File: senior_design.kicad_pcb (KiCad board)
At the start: 2 copper layers, 128.6 x 80.8 mm, 95 parts, among them J1 Conn_ARM_JTAG_SWD_20, J2 Conn_01x03_Pin, J4 USB_B_Micro, J5 Out_to_display, SW1 SW_SPST, U1 Boost Converter - TPS61169DCKR, U11 NCP1117-3.3_SOT223, U2 OPA196xDGK, U3 RA8875L3N, U4 OPA196xDGK, U5 M24C64-WMN6TP, U6 STM32F469VETx, U7 74HC4050D, Y1 20MHz

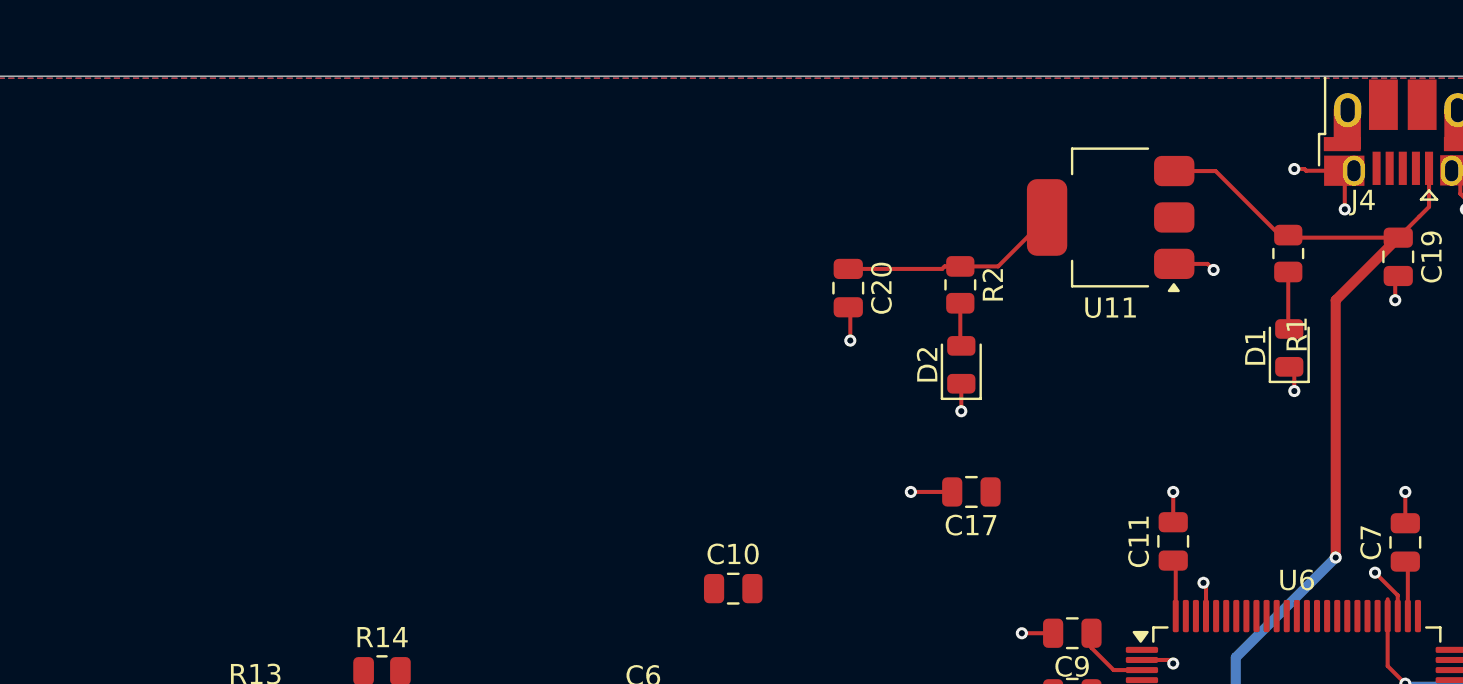
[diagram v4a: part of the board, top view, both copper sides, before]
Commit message: Updated Audio Schematic & PCB
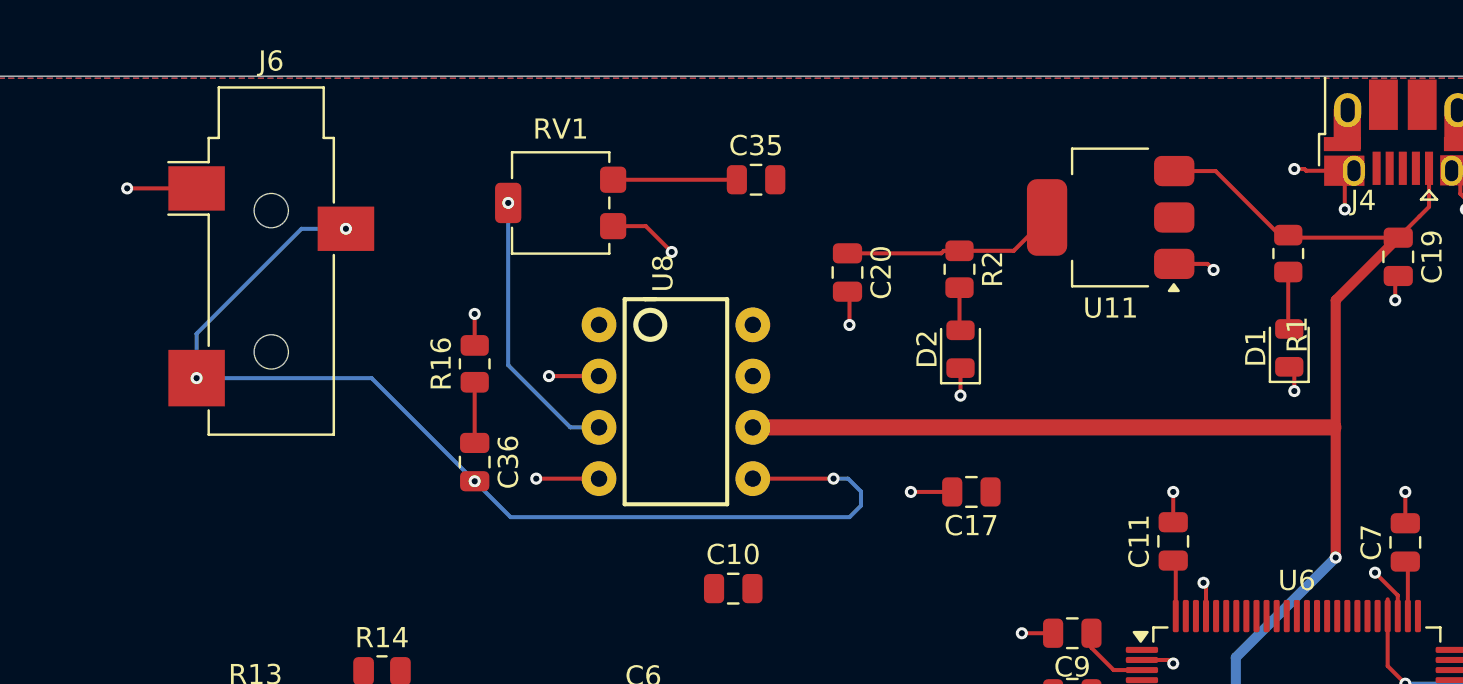
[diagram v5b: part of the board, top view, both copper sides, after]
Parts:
- added C35: 10 uF, Capacitor_SMD:C_0805_2012Metric, F.Cu at (166.8, 55.0)
- added C36: 0.1 uF, Capacitor_SMD:C_0805_2012Metric, F.Cu at (152.9, 69.0)
- added J6: AudioJack3, Connector_Audio:Jack_3.5mm_CUI_SJ-3523-SMT_Horizontal, F.Cu at (142.8, 59.1)
- added R16: 10 Ω, Resistor_SMD:R_0805_2012Metric, F.Cu at (152.9, 64.2)
- added RV1: R_Potentiometer_US, Potentiometer_SMD:Potentiometer_Bourns_3214G_Horizontal, F.Cu at (157.2, 56.2)
- added U8: LM386, Library:LM386, F.Cu at (162.9, 66.0)
- moved C20 0.77 mm to (171.4, 59.6)
- moved D2 0.77 mm to (177.0, 63.4)
- moved R2 0.77 mm to (176.9, 59.5)
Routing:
- net Net-(C36-Pad2): track 0.00 -> 54.1 mm, vias 0 -> 4
- net +5V: track 92.7 -> 121.6 mm
- net GND: track 157.7 -> 171.7 mm, vias 74 -> 79
- net Net-(U8-+): track 0.00 -> 13.8 mm, vias 0 -> 1
- net Net-(C35-Pad1): track 0.00 -> 6.13 mm
- net Net-(C36-Pad1): track 0.00 -> 3.00 mm

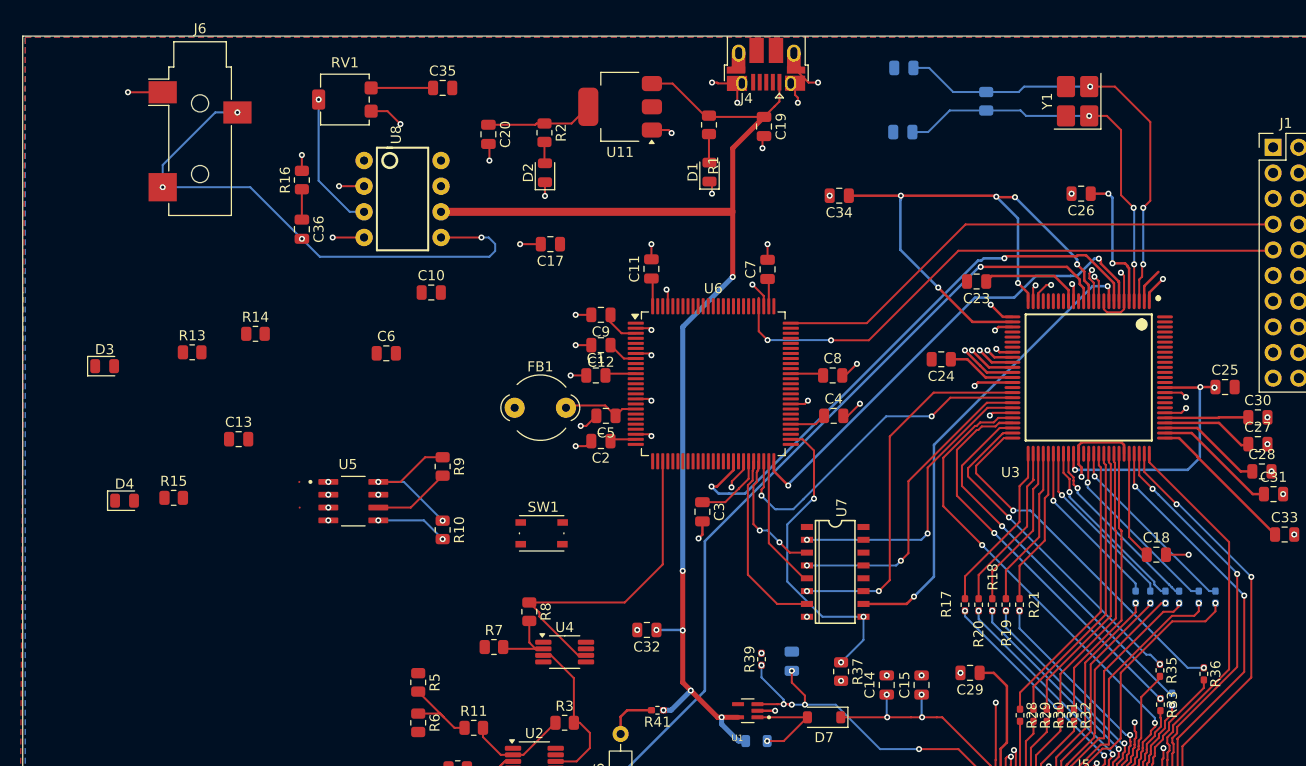
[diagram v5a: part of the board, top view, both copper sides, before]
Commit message: added memory and fixed clock
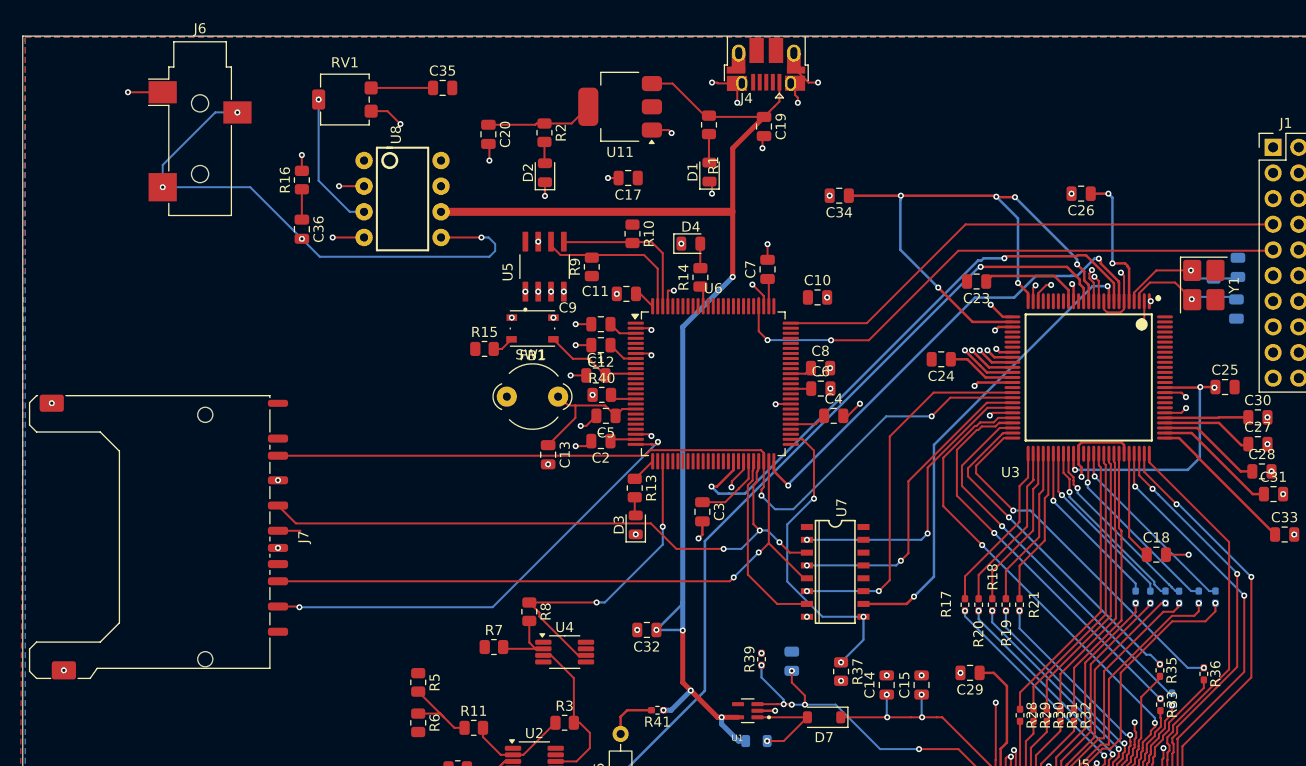
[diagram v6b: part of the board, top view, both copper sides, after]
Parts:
- added J7: SD_Card_Receptacle, Connector_Card:SD_Kyocera_145638009211859+, F.Cu at (138.0, 99.5)
- added R40: 0, Resistor_SMD:R_0805_2012Metric, F.Cu at (182.6, 85.4)
- moved D4 61.6 mm to (191.4, 70.5)
- moved D3 54.9 mm to (185.9, 98.3), turned to 90 degrees
- moved R13 45.8 mm to (185.8, 94.7), turned to -90 degrees
- moved R14 44.4 mm to (192.3, 73.8), turned to 90 degrees
- moved C6 43.2 mm to (204.3, 84.8)
- moved C21 40.7 mm to (245.4, 76.9), turned to 90 degrees
- moved C10 38.3 mm to (203.9, 75.8)
- moved C22 35.8 mm to (245.6, 72.8), turned to -90 degrees
- moved R10 34.8 mm to (185.6, 69.5)
- moved R15 34.1 mm to (171.0, 80.9)
- moved C13 30.7 mm to (177.3, 91.3), turned to -90 degrees
- moved U5 30.0 mm to (176.9, 72.7), turned to 90 degrees
- moved R38 29.1 mm to (243.2, 74.8), turned to 90 degrees
- moved R9 24.7 mm to (181.6, 72.8), turned to 90 degrees
- moved Y1 22.1 mm to (242.2, 74.5), turned to -90 degrees
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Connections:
- net /MCU/MISO renamed SPI_MISO
- net /MCU/MOSI renamed SPI_MOSI
- net /MCU/SCK renamed SPI_SCLK
- U6 pad 16: GND -> /MCU/VSSA
- U6 pad 25: unconnected-(U6-PA4-Pad25) -> SPI_SSD
- U6 pad 26: unconnected-(U6-PA5-Pad26) -> /MCU/LED1
- U6 pad 37: /MCU/LED1 -> unconnected-(U6-PE12-Pad37)
- U6 pad 98: unconnected-(U6-PB8-Pad98) -> I2C1_SDA
- U6 pad 99: unconnected-(U6-PB9-Pad99) -> I2C1_SCL
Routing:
- net SPI_SCLK: track 12.9 -> 63.3 mm, vias 2 -> 3
- net SPI_MOSI: track 13.3 -> 63.6 mm, vias 0 -> 2
- net SPI_MISO: track 33.5 -> 82.8 mm
- net SPI_SSD: track 0.00 -> 47.3 mm, vias 0 -> 2
- net /Peripherals/X_1: track 44.4 -> 11.8 mm, vias 3 -> 1
- net /Peripherals/X_0: track 39.8 -> 12.6 mm, vias 3 -> 1
- net +3.3V: track 187.7 -> 170.5 mm, vias 9 -> 7
- net /MCU/SWD_RESET: track 3.07 -> 11.9 mm
- net GND: track 171.7 -> 163.0 mm, vias 79 -> 90
- net I2C1_SDA: track 7.14 -> 15.5 mm, vias 2 -> 0
- net I2C1_SCL: track 7.68 -> 15.6 mm
- net /MCU/VDDA: track 7.88 -> 13.8 mm
- net +5V: track 121.6 -> 125.4 mm, vias 7 -> 6
- net /MCU/VSSA: track 0.00 -> 2.62 mm
- net /MCU/LED1: track 0.00 -> 2.49 mm
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
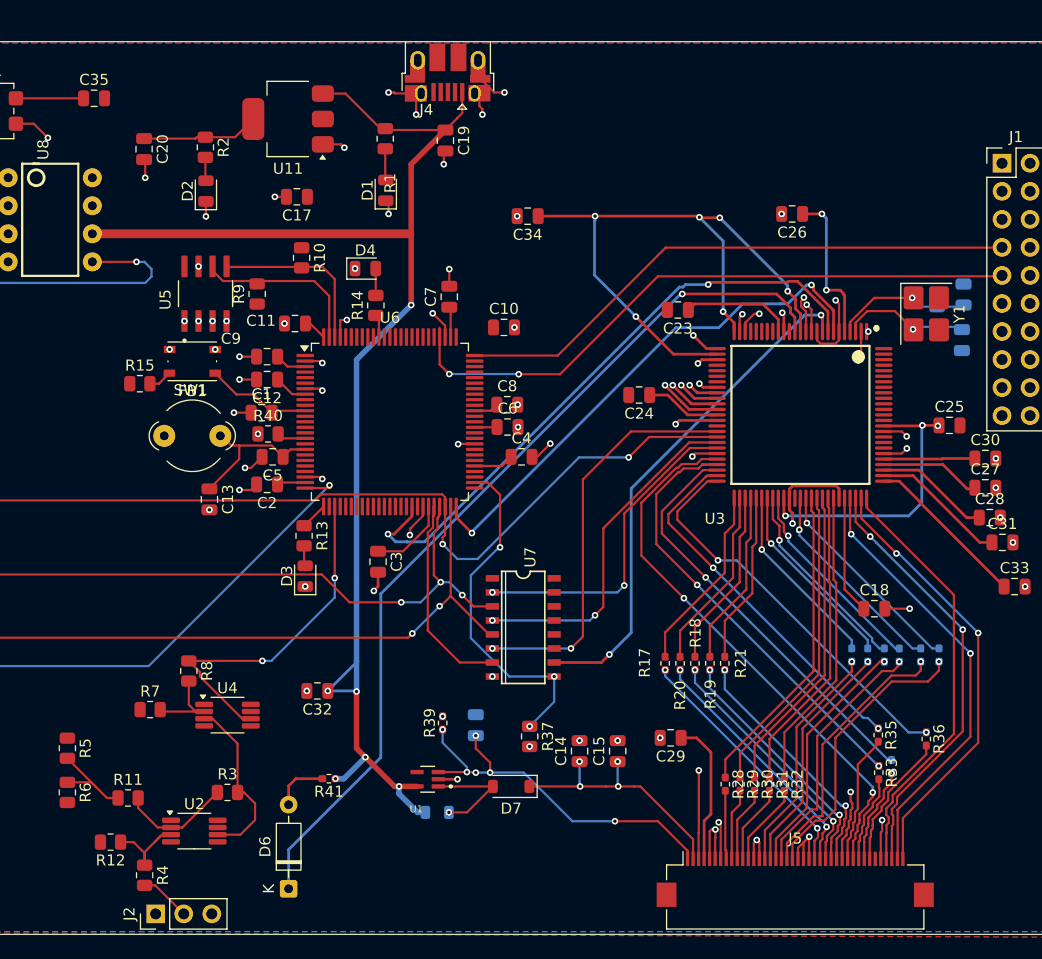
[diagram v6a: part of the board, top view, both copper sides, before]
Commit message: Fixed DRC errors
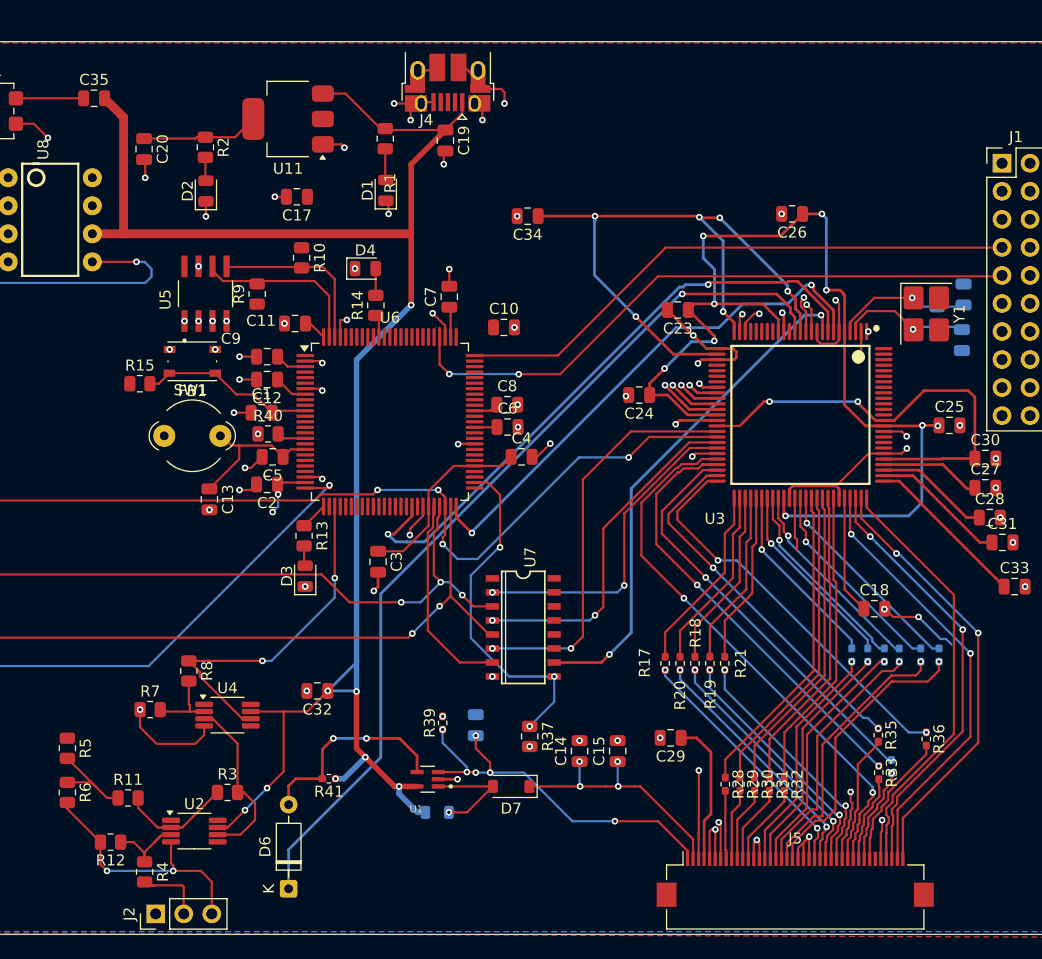
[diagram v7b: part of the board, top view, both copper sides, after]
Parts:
- moved J4 0.91 mm to (198.8, 53.6)
- moved R4 0.30 mm to (171.4, 125.1)
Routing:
- net GND: track 163.0 -> 216.3 mm, vias 90 -> 95
- net +3.3V: track 170.5 -> 216.5 mm, vias 7 -> 11
- net +1V5: track 57.4 -> 97.1 mm, vias 5 -> 9
- net +5V: track 125.4 -> 158.7 mm, vias 6 -> 8
- net Net-(D6-A): track 5.02 -> 18.8 mm, vias 0 -> 2
- net /MCU/SWD_RESET: track 11.9 -> 16.0 mm
- net Net-(J2-Pin_2): track 4.61 -> 7.00 mm
- net Net-(U4--): track 8.33 -> 7.39 mm
- net SPI_MISO: track 82.8 -> 83.1 mm, vias 2 -> 4

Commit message: Updated Schematic
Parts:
- added C37: 250 uF, Capacitor_SMD:C_0805_2012Metric, F.Cu at (145.6, 70.1)
- C31: value .01uF -> 0.1uF
- moved D3 2.19 mm to (186.6, 100.4)
- moved R13 1.47 mm to (186.6, 95.9)
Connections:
- C35 pad 2: +5V -> DAC_OUT1
- J2 pad 2: Net-(J2-Pin_2) -> GND
- J2 pad 3: GND -> Net-(J2-Pin_3)
- J6 pad R: Net-(C36-Pad2) -> Net-(C37-Pad2)
- J6 pad T: Net-(C36-Pad2) -> Net-(C37-Pad2)
- R4 pad 2: Net-(J2-Pin_2) -> Net-(J2-Pin_3)
- U6 pad 26: /MCU/LED1 -> DAC_OUT1
- U6 pad 27: unconnected-(U6-PA6-Pad27) -> /MCU/LED1
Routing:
- net DAC_OUT1: track 0.00 -> 62.3 mm, vias 0 -> 2
- net Net-(C36-Pad2): track 54.1 -> 24.6 mm, vias 4 -> 0
- net Net-(C37-Pad2): track 0.00 -> 19.4 mm, vias 0 -> 3
- net +5V: track 158.7 -> 145.7 mm
- net Net-(J2-Pin_3): track 0.00 -> 8.79 mm, vias 0 -> 2
- net Net-(J2-Pin_2): track 7.00 -> 0.00 mm
- net GND: track 216.3 -> 213.8 mm
- net /MCU/LED1: track 2.49 -> 3.64 mm
- net Net-(D3-A): track 1.84 -> 2.63 mm, vias 0 -> 2
